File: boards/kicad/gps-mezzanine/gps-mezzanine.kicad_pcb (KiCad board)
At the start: 2 copper layers, 55 x 54 mm, 18 parts, among them J1 CONN_01X04, P1 CONN_02X20, U1 MCP1700T-3302E/TT, U2 FGPMMOPA6H, U3 TXS0104E

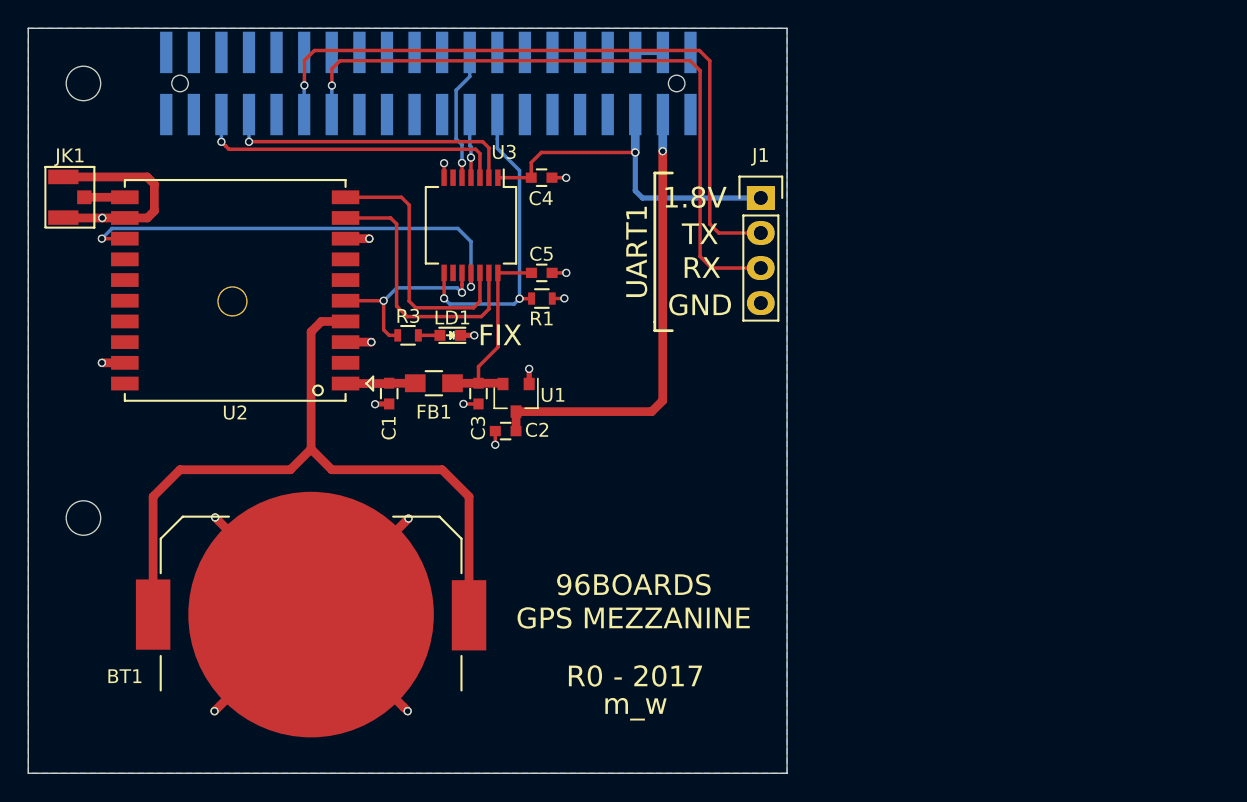
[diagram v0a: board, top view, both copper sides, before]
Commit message: Increase board size to full form factor
To make room for prototyping area and possible USB UART.

Signed-off-by: Michael Welling <mwelling@ieee.org>
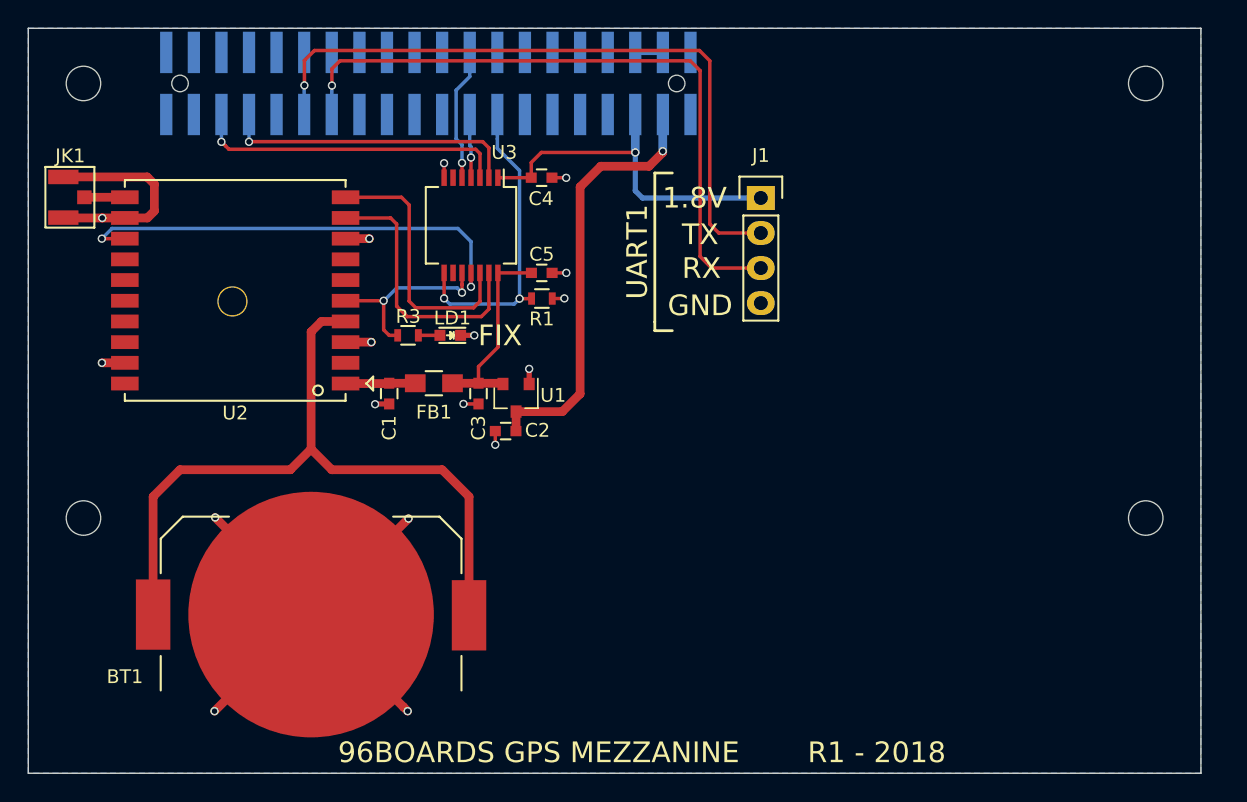
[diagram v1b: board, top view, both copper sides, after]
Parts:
- added MH3: M2.5, Mounting_Holes:MountingHole_2-5mm, F.Cu at (181.0, 104.0)
- added MH4: M2.5, Mounting_Holes:MountingHole_2-5mm, F.Cu at (181.0, 135.5)
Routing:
- net +5V: track 33.1 -> 31.4 mm
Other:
- board size 55 x 54 mm -> 85 x 54 mm
- board text added: "R1 - 2018"
- board text removed: "R0 - 2017"
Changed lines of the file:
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@@
   (general
     (thickness 1.6)
-    (drawings 23)
-    (tracks 187)
+    (drawings 24)
+    (tracks 191)
     (zones 0)
-    (modules 18)
+    (modules 20)
     (nets 57)
   )
@@
   )
   (setup
-    (last_trace_width 0.254)
+    (last_trace_width 0.635)
     (user_trace_width 0.254)
     (user_trace_width 0.381)
@@
     (add_net GND)
   )
+  (module Mounting_Holes:MountingHole_2-5mm (layer F.Cu)
+    (at 181 104)
+    (descr "Mounting hole, Befestigungsbohrung, 2,5mm, No Annular, Kein Restring,")
+    (tags "Mounting hole, Befestigungsbohrung, 2,5mm, No Annular, Kein Restring,")
+    (fp_text reference MH3 (at 0 -3.50012) (layer F.SilkS) hide
+      (effects (font (size 1 1) (thickness 0.15)))
+    )
+    (fp_text value M2.5 (at 0.09906 3.59918) (layer F.Fab) hide
+      (effects (font (size 1 1) (thickness 0.15)))
+    )
+    (fp_circle (center 0 0) (end 2.5 0) (layer Cmts.User) (width 0.381))
+    (pad 1 thru_hole circle (at 0 0) (size 2.5 2.5) (drill 2.5) (layers))
+  )
+  (module Mounting_Holes:MountingHole_2-5mm (layer F.Cu)
+    (at 181 135.5)
+    (descr "Mounting hole, Befestigungsbohrung, 2,5mm, No Annular, Kein Restring,")
+    (tags "Mounting hole, Befestigungsbohrung, 2,5mm, No Annular, Kein Restring,")
+    (fp_text reference MH4 (at 0 -3.50012) (layer F.SilkS) hide
+      (effects (font (size 1 1) (thickness 0.15)))
+    )
+    (fp_text value M2.5 (at 0.09906 3.59918) (layer F.Fab) hide
+      (effects (font (size 1 1) (thickness 0.15)))
+    )
+    (fp_circle (center 0 0) (end 2.5 0) (layer Cmts.User) (width 0.381))
+    (pad 1 thru_hole circle (at 0 0) (size 2.5 2.5) (drill 2.5) (layers))
+  )
   (module 96boards:FGPMMOPA6H (layer F.Cu)
     (at 115 119 180)
@@
     )
   )
+  (dimension 81 (width 0.3) (layer F.Fab)
+    (gr_text "81.000 mm" (at 140.5 87.15) (layer F.Fab)
+      (effects (font (size 1.5 1.5) (thickness 0.3)))
+    )
+    (feature1 (pts (xy 181 104) (xy 181 85.8)))
+    (feature2 (pts (xy 100 104) (xy 100 85.8)))
+    (crossbar (pts (xy 100 88.5) (xy 181 88.5)))
+    (arrow1a (pts (xy 181 88.5) (xy 179.873496 89.086421)))
+    (arrow1b (pts (xy 181 88.5) (xy 179.873496 87.913579)))
+    (arrow2a (pts (xy 100 88.5) (xy 101.126504 89.086421)))
+    (arrow2b (pts (xy 100 88.5) (xy 101.126504 87.913579)))
+  )
   (gr_line (start 145.415 121.92) (end 146.685 121.92) (layer F.SilkS) (width 0.2))
   (gr_line (start 145.415 121.285) (end 145.415 121.92) (layer F.SilkS) (width 0.2))
@@
     (effects (font (size 1.5 1.5) (thickness 0.3)))
   )
-  (gr_text m_w (at 144 149) (layer F.SilkS)
-    (effects (font (size 1.5 1.5) (thickness 0.3)))
-  )
-  (gr_text "96BOARDS\nGPS MEZZANINE" (at 143.89 141.59) (layer F.SilkS)
+  (gr_text m_w (at 181.5 152.5) (layer B.SilkS)
+    (effects (font (size 1.5 1.5) (thickness 0.3)) (justify mirror))
+  )
+  (gr_text "96BOARDS GPS MEZZANINE" (at 137 152.5) (layer F.SilkS)
     (effects (font (size 1.5 1.5) (thickness 0.3)))
   )
@@
     (arrow2b (pts (xy 97.5 135.5) (xy 96.913579 134.373496)))
   )
-  (gr_text "R0 - 2017" (at 144 147) (layer F.SilkS)
+  (gr_text "R1 - 2018" (at 161.5 152.5) (layer F.SilkS)
     (effects (font (size 1.5 1.5) (thickness 0.3)))
   )
@@
     (arrow2b (pts (xy 100 95) (xy 101.126504 94.413579)))
   )
-  (dimension 55 (width 0.3) (layer F.Fab)
-    (gr_text "55.000 mm" (at 127.5 88.65) (layer F.Fab)
+  (dimension 85 (width 0.3) (layer F.Fab)
+    (gr_text "85.000 mm" (at 142.5 82.15) (layer F.Fab)
       (effects (font (size 1.5 1.5) (thickness 0.3)))
     )
-    (feature1 (pts (xy 155 100) (xy 155 87.3)))
-    (feature2 (pts (xy 100 100) (xy 100 87.3)))
-    (crossbar (pts (xy 100 90) (xy 155 90)))
-    (arrow1a (pts (xy 155 90) (xy 153.873496 90.586421)))
-    (arrow1b (pts (xy 155 90) (xy 153.873496 89.413579)))
-    (arrow2a (pts (xy 100 90) (xy 101.126504 90.586421)))
-    (arrow2b (pts (xy 100 90) (xy 101.126504 89.413579)))
+    (feature1 (pts (xy 185 100) (xy 185 80.8)))
+    (feature2 (pts (xy 100 100) (xy 100 80.8)))
+    (crossbar (pts (xy 100 83.5) (xy 185 83.5)))
+    (arrow1a (pts (xy 185 83.5) (xy 183.873496 84.086421)))
+    (arrow1b (pts (xy 185 83.5) (xy 183.873496 82.913579)))
+    (arrow2a (pts (xy 100 83.5) (xy 101.126504 84.086421)))
+    (arrow2b (pts (xy 100 83.5) (xy 101.126504 82.913579)))
   )
   (dimension 54 (width 0.3) (layer F.Fab)
@@
     (arrow2b (pts (xy 90 154) (xy 89.413579 152.873496)))
   )
-  (gr_line (start 100 154) (end 155 154) (angle 90) (layer Edge.Cuts) (width 0.1))
-  (gr_line (start 155 100) (end 155 154) (angle 90) (layer Edge.Cuts) (width 0.1))
+  (gr_line (start 100 154) (end 185 154) (angle 90) (layer Edge.Cuts) (width 0.1))
+  (gr_line (start 185 100) (end 185 154) (angle 90) (layer Edge.Cuts) (width 0.1))
   (gr_line (start 100 154) (end 100 100) (angle 90) (layer Edge.Cuts) (width 0.1))
-  (gr_line (start 100 100) (end 155 100) (angle 90) (layer Edge.Cuts) (width 0.1))
+  (gr_line (start 100 100) (end 185 100) (angle 90) (layer Edge.Cuts) (width 0.1))
   (segment (start 144.52 112.3) (end 153.1 112.3) (width 0.381) (layer B.Cu) (net 1))
   (segment (start 144 111.78) (end 144.52 112.3) (width 0.381) (layer B.Cu) (net 1))
@@
   (segment (start 105.36292 113.75) (end 105.36174 113.74882) (width 0.635) (layer F.Cu) (net 2))
   (via (at 105.36174 113.74882) (size 0.6) (drill 0.4) (layers F.Cu B.Cu) (net 2))
-  (segment (start 145.194785 127.785215) (end 135.357915 127.785215) (width 0.635) (layer F.Cu) (net 3))
-  (segment (start 145.194785 127.785215) (end 145.98904 126.99096) (width 0.635) (layer F.Cu) (net 3))
-  (segment (start 145.98904 126.99096) (end 145.98904 108.91266) (width 0.635) (layer F.Cu) (net 3))
+  (segment (start 135.357915 127.785215) (end 138.714785 127.785215) (width 0.635) (layer F.Cu) (net 3))
+  (segment (start 140 111.5) (end 141.5 110) (width 0.635) (layer F.Cu) (net 3))
+  (segment (start 145.98904 109.01096) (end 145.98904 108.91266) (width 0.635) (layer F.Cu) (net 3))
+  (segment (start 138.714785 127.785215) (end 140 126.5) (width 0.635) (layer F.Cu) (net 3))
+  (segment (start 140 126.5) (end 140 111.5) (width 0.635) (layer F.Cu) (net 3))
+  (segment (start 141.5 110) (end 145 110) (width 0.635) (layer F.Cu) (net 3))
+  (segment (start 145 110) (end 145.98904 109.01096) (width 0.635) (layer F.Cu) (net 3))
   (segment (start 135.357915 127.785215) (end 135.357915 129.191405) (width 0.635) (layer F.Cu) (net 3))
   (segment (start 135.357915 129.191405) (end 135.35222 129.1971) (width 0.635) (layer F.Cu) (net 3))
@@
     (polygon
       (pts
-        (xy 100 100) (xy 155 100) (xy 155 154) (xy 100 154)
+        (xy 100 100) (xy 185 100) (xy 185 154) (xy 100 154)
       )
     )

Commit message: Add headers, proto area, and route
Signed-off-by: Michael Welling <mwelling@ieee.org>
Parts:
- added C10: 1uF, Capacitors_SMD:C_0603, F.Cu at (161.5, 144.7)
- added C11: .1uF, Capacitors_SMD:C_0603, F.Cu at (164.5, 152.2)
- added C6: 4.7uF, Capacitors_SMD:C_0603, F.Cu at (172.5, 152.2)
- added C7: 47pF, Capacitors_SMD:C_0603, F.Cu at (177.7, 148.9)
- added C8: 47pF, Capacitors_SMD:C_0603, F.Cu at (177.7, 145.9)
- added C9: 1uF, Capacitors_SMD:C_0603, F.Cu at (161.5, 149.9)
- added FB2: ILBB0805ER102V, Resistors_SMD:R_0805_HandSoldering, F.Cu at (176.2, 152.1)
- added J2: CONN_02X06, Pin_Headers:Pin_Header_Straight_2x06, F.Cu at (152.3, 106.7)
- added J3: CONN_02X06, Pin_Headers:Pin_Header_Straight_2x06, F.Cu at (179.1, 114.3)
- added R2: 10K, Resistors_SMD:R_0603, F.Cu at (167.4, 152.3)
- added R4: 27, Resistors_SMD:R_0603, F.Cu at (175.3, 146.6)
- added R5: 27, Resistors_SMD:R_0603, F.Cu at (175.3, 148.2)
- added R6: 220, Resistors_SMD:R_0603, F.Cu at (165.5, 143.0)
- added R7: 220, Resistors_SMD:R_0603, F.Cu at (169.7, 152.3)
- added REF**: pad, 96boards:pad, F.Cu at (142.2, 129.5)
- added REF**: pad, 96boards:pad, F.Cu at (142.2, 124.5)
- added REF**: pad, 96boards:pad, F.Cu at (154.9, 132.1)
- added REF**: pad, 96boards:pad, F.Cu at (167.6, 132.1)
- added REF**: pad, 96boards:pad, F.Cu at (172.7, 132.1)
- added REF**: pad, 96boards:pad, F.Cu at (160.0, 132.1)
- added REF**: pad, 96boards:pad, F.Cu at (170.2, 132.1)
- added REF**: pad, 96boards:pad, F.Cu at (157.5, 132.1)
- added REF**: pad, 96boards:pad, F.Cu at (165.1, 132.1)
- added REF**: pad, 96boards:pad, F.Cu at (147.3, 132.1)
- added REF**: pad, 96boards:pad, F.Cu at (162.6, 132.1)
- added REF**: pad, 96boards:pad, F.Cu at (149.9, 132.1)
- added REF**: pad, 96boards:pad, F.Cu at (142.2, 139.7)
- added REF**: pad, 96boards:pad, F.Cu at (152.4, 132.1)
- added REF**: pad, 96boards:pad, F.Cu at (167.6, 134.6)
- added REF**: pad, 96boards:pad, F.Cu at (147.3, 134.6)
- added REF**: pad, 96boards:pad, F.Cu at (157.5, 134.6)
- added REF**: pad, 96boards:pad, F.Cu at (165.1, 134.6)
- added REF**: pad, 96boards:pad, F.Cu at (170.2, 134.6)
- added REF**: pad, 96boards:pad, F.Cu at (160.0, 134.6)
- added REF**: pad, 96boards:pad, F.Cu at (162.6, 134.6)
- added REF**: pad, 96boards:pad, F.Cu at (154.9, 134.6)
- added REF**: pad, 96boards:pad, F.Cu at (149.9, 134.6)
- added REF**: pad, 96boards:pad, F.Cu at (157.5, 114.3)
- added REF**: pad, 96boards:pad, F.Cu at (172.7, 134.6)
- added REF**: pad, 96boards:pad, F.Cu at (152.4, 134.6)
- added REF**: pad, 96boards:pad, F.Cu at (154.9, 139.7)
- added REF**: pad, 96boards:pad, F.Cu at (149.9, 139.7)
- added REF**: pad, 96boards:pad, F.Cu at (152.4, 139.7)
- added REF**: pad, 96boards:pad, F.Cu at (167.6, 139.7)
- added REF**: pad, 96boards:pad, F.Cu at (165.1, 139.7)
- added REF**: pad, 96boards:pad, F.Cu at (170.2, 139.7)
- added REF**: pad, 96boards:pad, F.Cu at (172.7, 139.7)
- added REF**: pad, 96boards:pad, F.Cu at (162.6, 139.7)
- added REF**: pad, 96boards:pad, F.Cu at (160.0, 114.3)
- added REF**: pad, 96boards:pad, F.Cu at (160.0, 139.7)
- added REF**: pad, 96boards:pad, F.Cu at (157.5, 139.7)
- added REF**: pad, 96boards:pad, F.Cu at (147.3, 139.7)
- added REF**: pad, 96boards:pad, F.Cu at (147.3, 137.2)
- added REF**: pad, 96boards:pad, F.Cu at (149.9, 137.2)
- added REF**: pad, 96boards:pad, F.Cu at (152.4, 137.2)
- added REF**: pad, 96boards:pad, F.Cu at (154.9, 137.2)
- added REF**: pad, 96boards:pad, F.Cu at (157.5, 137.2)
- added REF**: pad, 96boards:pad, F.Cu at (160.0, 137.2)
- added REF**: pad, 96boards:pad, F.Cu at (162.6, 137.2)
- added REF**: pad, 96boards:pad, F.Cu at (149.9, 114.3)
- added REF**: pad, 96boards:pad, F.Cu at (165.1, 137.2)
- added REF**: pad, 96boards:pad, F.Cu at (167.6, 137.2)
- added REF**: pad, 96boards:pad, F.Cu at (170.2, 137.2)
- added REF**: pad, 96boards:pad, F.Cu at (172.7, 137.2)
- added REF**: pad, 96boards:pad, F.Cu at (147.3, 114.3)
- added REF**: pad, 96boards:pad, F.Cu at (165.1, 114.3)
- added REF**: pad, 96boards:pad, F.Cu at (152.4, 114.3)
- added REF**: pad, 96boards:pad, F.Cu at (162.6, 114.3)
- added REF**: pad, 96boards:pad, F.Cu at (170.2, 114.3)
- added REF**: pad, 96boards:pad, F.Cu at (142.2, 114.3)
- added REF**: pad, 96boards:pad, F.Cu at (172.7, 114.3)
- added REF**: pad, 96boards:pad, F.Cu at (144.8, 114.3)
- added REF**: pad, 96boards:pad, F.Cu at (154.9, 114.3)
- added REF**: pad, 96boards:pad, F.Cu at (167.6, 114.3)
- added REF**: pad, 96boards:pad, F.Cu at (172.7, 116.8)
- added REF**: pad, 96boards:pad, F.Cu at (147.3, 116.8)
- added REF**: pad, 96boards:pad, F.Cu at (154.9, 116.8)
- added REF**: pad, 96boards:pad, F.Cu at (149.9, 116.8)
- added REF**: pad, 96boards:pad, F.Cu at (165.1, 116.8)
- added REF**: pad, 96boards:pad, F.Cu at (160.0, 116.8)
- added REF**: pad, 96boards:pad, F.Cu at (142.2, 127.0)
- added REF**: pad, 96boards:pad, F.Cu at (162.6, 116.8)
- added REF**: pad, 96boards:pad, F.Cu at (170.2, 116.8)
- added REF**: pad, 96boards:pad, F.Cu at (144.8, 116.8)
- added REF**: pad, 96boards:pad, F.Cu at (152.4, 116.8)
- added REF**: pad, 96boards:pad, F.Cu at (167.6, 116.8)
- added REF**: pad, 96boards:pad, F.Cu at (157.5, 116.8)
- added REF**: pad, 96boards:pad, F.Cu at (170.2, 119.4)
- added REF**: pad, 96boards:pad, F.Cu at (152.4, 119.4)
- added REF**: pad, 96boards:pad, F.Cu at (149.9, 119.4)
- added REF**: pad, 96boards:pad, F.Cu at (144.8, 119.4)
- added REF**: pad, 96boards:pad, F.Cu at (142.2, 137.2)
- added REF**: pad, 96boards:pad, F.Cu at (165.1, 119.4)
- added REF**: pad, 96boards:pad, F.Cu at (172.7, 119.4)
- added REF**: pad, 96boards:pad, F.Cu at (160.0, 119.4)
- added REF**: pad, 96boards:pad, F.Cu at (162.6, 119.4)
- added REF**: pad, 96boards:pad, F.Cu at (157.5, 119.4)
- added REF**: pad, 96boards:pad, F.Cu at (154.9, 119.4)
- added REF**: pad, 96boards:pad, F.Cu at (147.3, 119.4)
- added REF**: pad, 96boards:pad, F.Cu at (167.6, 119.4)
- added REF**: pad, 96boards:pad, F.Cu at (160.0, 121.9)
- added REF**: pad, 96boards:pad, F.Cu at (172.7, 121.9)
- added REF**: pad, 96boards:pad, F.Cu at (142.2, 121.9)
- added REF**: pad, 96boards:pad, F.Cu at (167.6, 121.9)
- added REF**: pad, 96boards:pad, F.Cu at (152.4, 121.9)
- added REF**: pad, 96boards:pad, F.Cu at (165.1, 121.9)
- added REF**: pad, 96boards:pad, F.Cu at (170.2, 121.9)
- added REF**: pad, 96boards:pad, F.Cu at (149.9, 121.9)
- added REF**: pad, 96boards:pad, F.Cu at (144.8, 121.9)
- added REF**: pad, 96boards:pad, F.Cu at (162.6, 121.9)
- added REF**: pad, 96boards:pad, F.Cu at (147.3, 121.9)
- added REF**: pad, 96boards:pad, F.Cu at (157.5, 121.9)
- added REF**: pad, 96boards:pad, F.Cu at (154.9, 121.9)
- added REF**: pad, 96boards:pad, F.Cu at (142.2, 119.4)
- added REF**: pad, 96boards:pad, F.Cu at (149.9, 124.5)
- added REF**: pad, 96boards:pad, F.Cu at (167.6, 124.5)
- added REF**: pad, 96boards:pad, F.Cu at (144.8, 124.5)
- added REF**: pad, 96boards:pad, F.Cu at (157.5, 124.5)
- added REF**: pad, 96boards:pad, F.Cu at (165.1, 124.5)
- added REF**: pad, 96boards:pad, F.Cu at (172.7, 124.5)
- added REF**: pad, 96boards:pad, F.Cu at (147.3, 124.5)
- added REF**: pad, 96boards:pad, F.Cu at (154.9, 124.5)
- added REF**: pad, 96boards:pad, F.Cu at (170.2, 124.5)
- added REF**: pad, 96boards:pad, F.Cu at (162.6, 124.5)
- added REF**: pad, 96boards:pad, F.Cu at (142.2, 132.1)
- added REF**: pad, 96boards:pad, F.Cu at (152.4, 124.5)
- added REF**: pad, 96boards:pad, F.Cu at (160.0, 124.5)
- added REF**: pad, 96boards:pad, F.Cu at (144.8, 132.1)
- added REF**: pad, 96boards:pad, F.Cu at (144.8, 139.7)
- added REF**: pad, 96boards:pad, F.Cu at (144.8, 129.5)
- added REF**: pad, 96boards:pad, F.Cu at (144.8, 127.0)
- added REF**: pad, 96boards:pad, F.Cu at (144.8, 134.6)
- added REF**: pad, 96boards:pad, F.Cu at (144.8, 137.2)
- added REF**: pad, 96boards:pad, F.Cu at (157.5, 127.0)
- added REF**: pad, 96boards:pad, F.Cu at (162.6, 127.0)
- added REF**: pad, 96boards:pad, F.Cu at (142.2, 134.6)
- added REF**: pad, 96boards:pad, F.Cu at (172.7, 127.0)
- added REF**: pad, 96boards:pad, F.Cu at (147.3, 127.0)
- added REF**: pad, 96boards:pad, F.Cu at (152.4, 127.0)
- added REF**: pad, 96boards:pad, F.Cu at (160.0, 127.0)
- added REF**: pad, 96boards:pad, F.Cu at (170.2, 127.0)
- added REF**: pad, 96boards:pad, F.Cu at (149.9, 127.0)
- added REF**: pad, 96boards:pad, F.Cu at (167.6, 127.0)
- added REF**: pad, 96boards:pad, F.Cu at (154.9, 127.0)
- added REF**: pad, 96boards:pad, F.Cu at (165.1, 127.0)
- added REF**: pad, 96boards:pad, F.Cu at (165.1, 129.5)
- added REF**: pad, 96boards:pad, F.Cu at (142.2, 116.8)
- added REF**: pad, 96boards:pad, F.Cu at (147.3, 129.5)
- added REF**: pad, 96boards:pad, F.Cu at (152.4, 129.5)
- added REF**: pad, 96boards:pad, F.Cu at (162.6, 129.5)
- added REF**: pad, 96boards:pad, F.Cu at (160.0, 129.5)
- added REF**: pad, 96boards:pad, F.Cu at (170.2, 129.5)
- added REF**: pad, 96boards:pad, F.Cu at (149.9, 129.5)
- added REF**: pad, 96boards:pad, F.Cu at (167.6, 129.5)
- added REF**: pad, 96boards:pad, F.Cu at (157.5, 129.5)
- added REF**: pad, 96boards:pad, F.Cu at (172.7, 129.5)
- added REF**: pad, 96boards:pad, F.Cu at (154.9, 129.5)
- added U4: FT230X, Housings_SSOP:SSOP-16_3.9x4.9mm_Pitch0.635mm, F.Cu at (167.8, 147.3)
- added U5: MCP1700T-1802E, TO_SOT_Packages_SMD:SOT-23, F.Cu at (161.5, 147.3)
- J1: value CONN_01X04 -> USB_OTG; footprint Pin_Headers:Pin_Header_Straight_1x04 -> Connect:USB_Micro-B
- moved J1 45.5 mm to (182.4, 147.1), turned to 90 degrees
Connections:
- J1 pad 1: +1V8 -> Net-(FB2-Pad2)
- J1 pad 2: UART1_TX -> Net-(C7-Pad1)
- J1 pad 3: UART1_RX -> Net-(C8-Pad1)
- J1 pad 4: GND -> Net-(J1-Pad4)
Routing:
- net RST_BTN_N: track 0.00 -> 105.5 mm, vias 0 -> 3
- net PWR_BTN_N: track 0.00 -> 89.7 mm, vias 0 -> 1
- net GPIO_H: track 0.00 -> 58.2 mm, vias 0 -> 1
- net GPIO_J: track 0.00 -> 57.4 mm, vias 0 -> 1
- net GPIO_I: track 0.00 -> 46.5 mm, vias 0 -> 1
- net +5V: track 31.4 -> 77.4 mm, vias 1 -> 2
- net GPIO_K: track 0.00 -> 45.8 mm, vias 0 -> 1
- net SPIO_DOUT: track 0.00 -> 42.2 mm, vias 0 -> 1
- net SPIO_CS: track 0.00 -> 41.6 mm, vias 0 -> 1
- net SPIO_DIN: track 0.00 -> 41.1 mm, vias 0 -> 1
- net SPIO_SCL: track 0.00 -> 39.9 mm, vias 0 -> 1
- net +1V8: track 26.2 -> 61.3 mm
- net I2C1_SDA: track 0.00 -> 33.9 mm, vias 0 -> 1
- net UART1_RX: track 48.8 -> 82.4 mm
- net I2C1_SCL: track 0.00 -> 33.4 mm, vias 0 -> 1
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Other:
- net class Default: clearance 0 -> 0.1524; trace_width 0.254 -> 0.1524
- rule trace_clearance: 0 -> 0.1524
- rule trace_min: 0.1778 -> 0.1524
- board text added: "5V"
- board text added: "CSn"
- board text added: "D"
- board text added: "E"
- board text added: "F"
- board text added: "G"
- board text added: "H"
- board text added: "I"
- board text added: "J"
- board text added: "K"
- board text added: "MISO"
- board text added: "MOSI"
- board text added: "SCK"
- board text added: "SCL0"
- board text added: "SCL1"
- board text added: "SDA0"
- board text added: "SDA1"
- board text removed: "RX"
- board text removed: "TX"
- board text removed: "UART1"

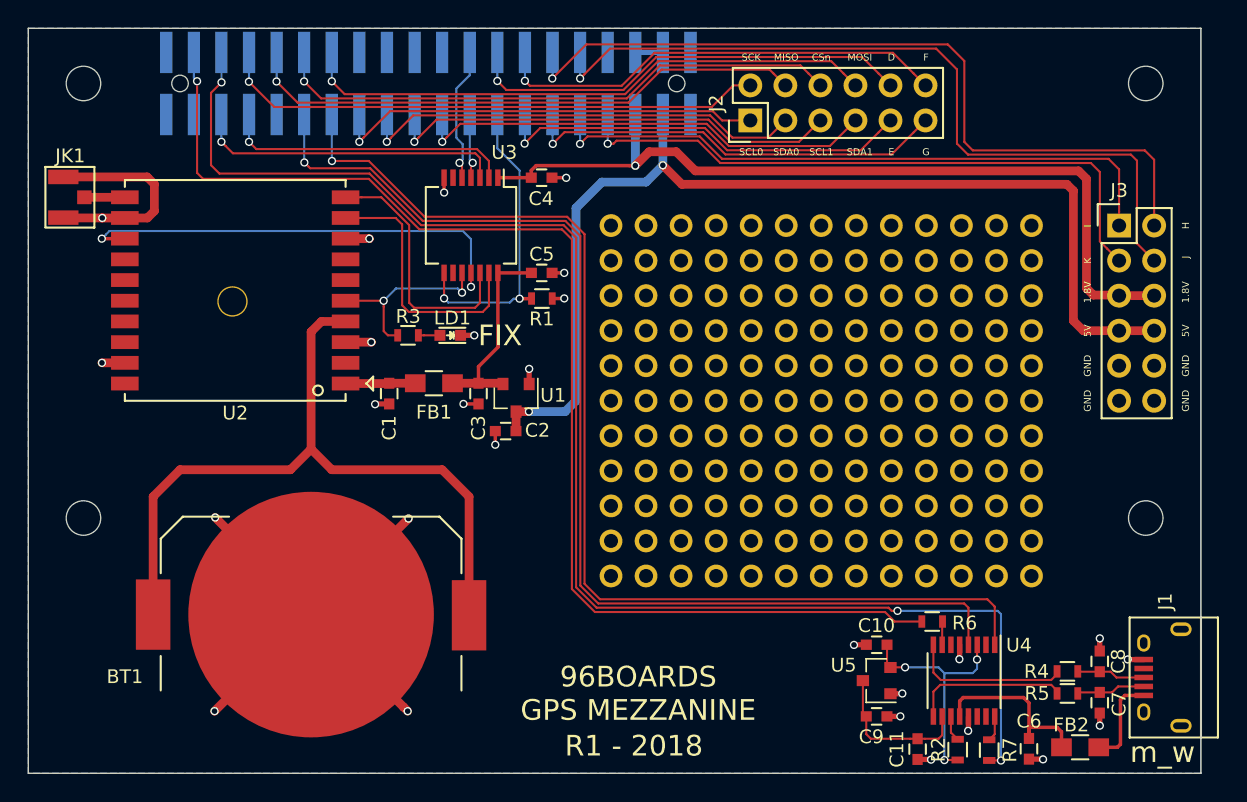
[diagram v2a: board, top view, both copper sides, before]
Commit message: Updates for maufacturing
Adds fiducials for manufacturing.
Switches to SMT USB connector.
Fixes pattern for the level translator.
Adds QWERTY logo to the bottom of the board.

Signed-off-by: Michael Welling <mwelling@ieee.org>
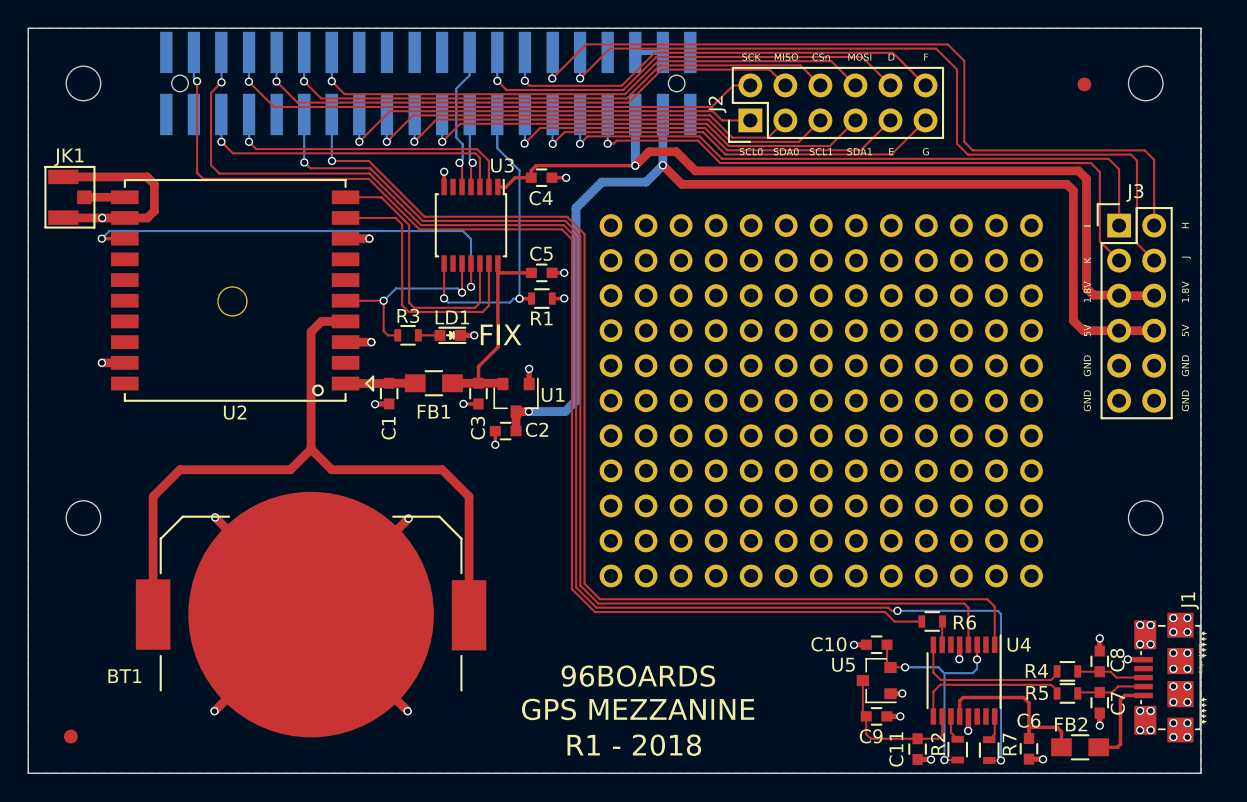
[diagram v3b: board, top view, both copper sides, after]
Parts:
- added *G1: FIDUCIAL, 96boards:Fiducial_1mm_Dia_2.00mm_Outer_CopperTop, F.Cu at (103.1, 151.3)
- added *G2: FIDUCIAL, 96boards:Fiducial_1mm_Dia_2.00mm_Outer_CopperTop, F.Cu at (176.6, 104.1)
- added G***: LOGO, 96boards:qwerty, B.Cu at (141.2, 146.5)
- J1: footprint Connect:USB_Micro-B -> 96boards:10118192-0001LF(MICRO-USB-B-AMPHENOL-FCI)
- U3: footprint Housings_SSOP:SSOP-14_5.3x6.2mm_Pitch0.65mm -> 96boards:TSSOP-14_4.3x5.1mm_Pitch0.65mm
- moved J1 1.10 mm to (183.5, 147.1)
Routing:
- net GPIO_B: track 9.84 -> 11.1 mm
- net UART0_TX: track 22.6 -> 23.7 mm
- net UART0_RX: track 21.2 -> 22.2 mm
- net GPIO_A: track 4.72 -> 5.73 mm
- net GPS_TX: track 19.2 -> 19.9 mm
- net GPS_RX: track 18.8 -> 19.5 mm
- net GPS_1PPS: track 33.4 -> 34.0 mm
- net GPIO_C: track 22.5 -> 23.1 mm
- net FIX: track 13.7 -> 14.4 mm
- net +3V3: track 14.7 -> 15.4 mm
- net GND: vias 27 -> 51
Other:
- net class Default: clearance 0.1524 -> 0
- rule trace_clearance: 0.1524 -> 0
- board text removed: "m_w"
